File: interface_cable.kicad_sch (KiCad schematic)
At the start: 18 parts

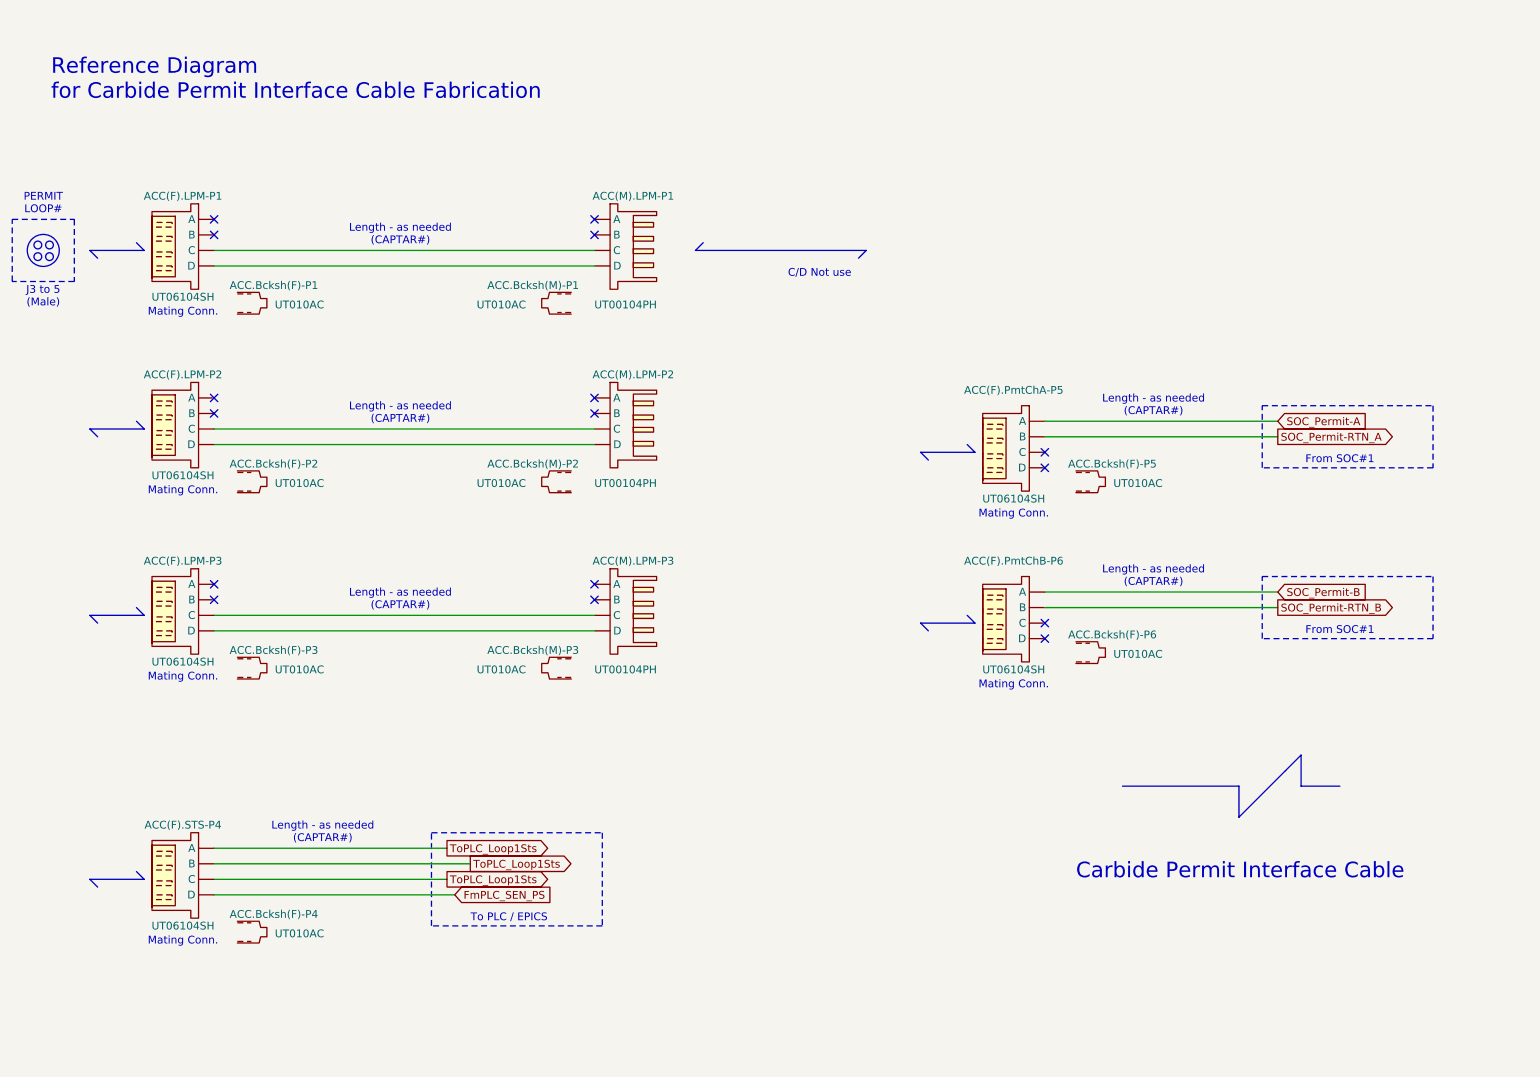
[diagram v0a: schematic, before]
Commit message: Updated Interface cable
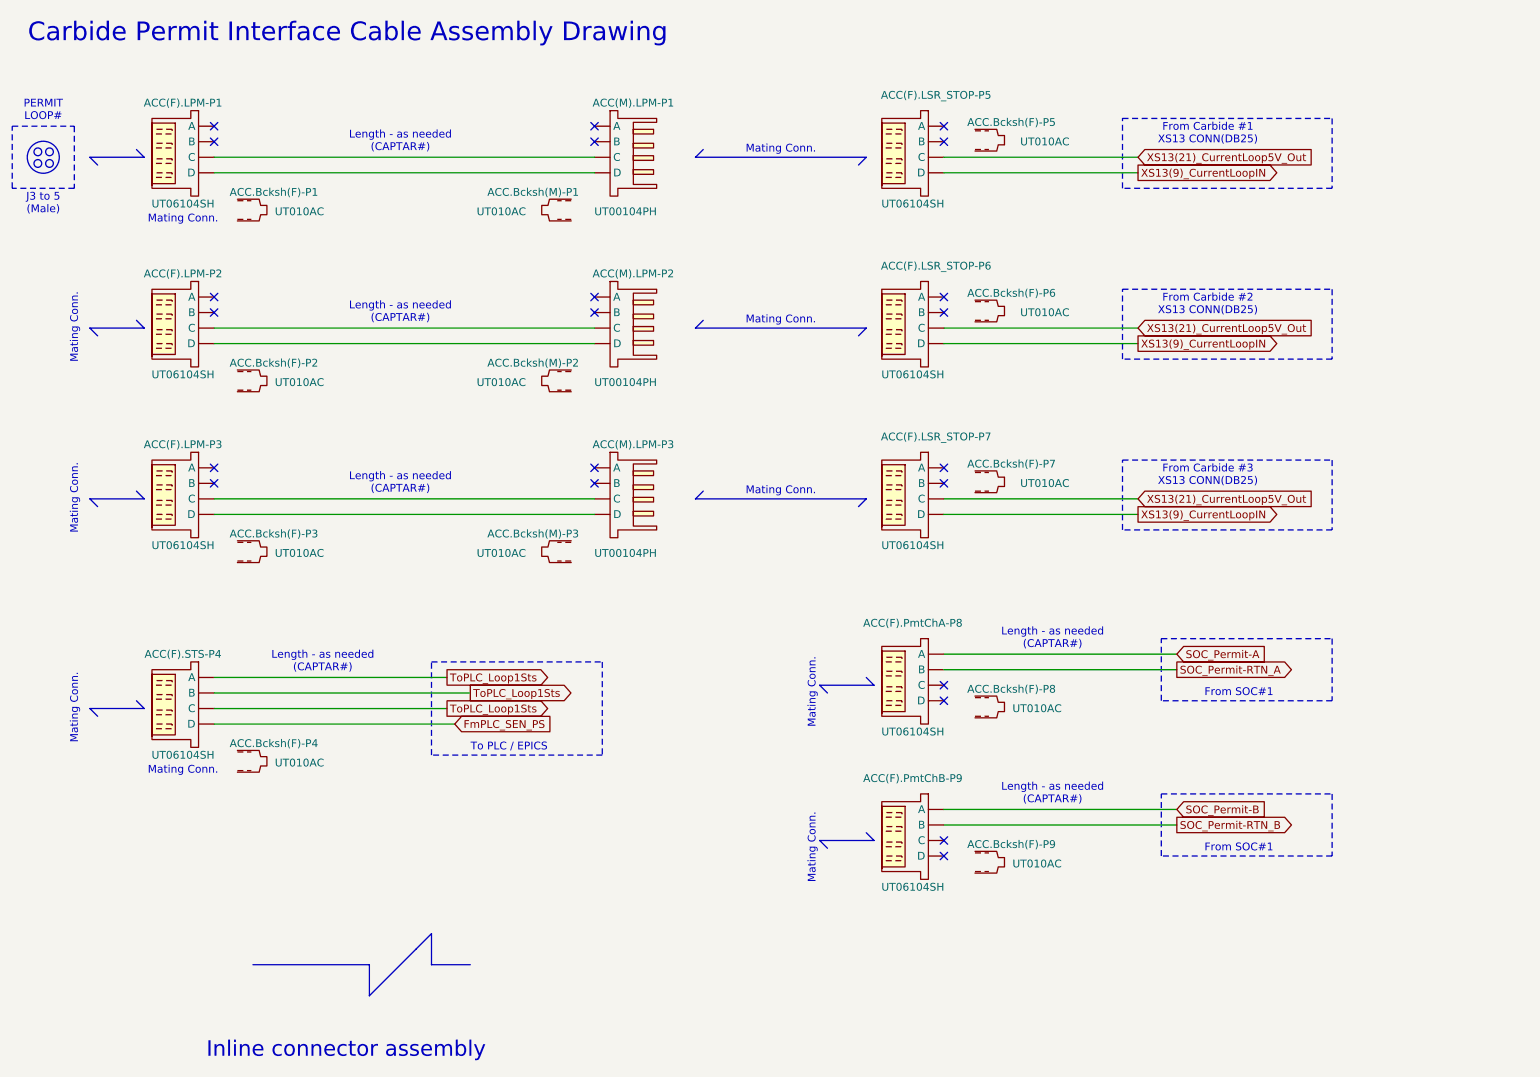
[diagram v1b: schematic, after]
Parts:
- added ACC(F).LSR_STOP-P5, ACC(F).LSR_STOP-P6, ACC(F).LSR_STOP-P7: UT06104SH, symbol JP_3xCarbide:CONN_UT00104SH(F)
- added ACC.Bcksh(F)-P5, ACC.Bcksh(F)-P6, ACC.Bcksh(F)-P7: UT010AC, symbol JP_3xCarbide:Bcksh_/_Clamp
- renumbered ACC(F).PmtChA-P5 to ACC(F).PmtChA-P8, ACC(F).PmtChB-P6 to ACC(F).PmtChB-P9, ACC.Bcksh(F)-P5 to ACC.Bcksh(F)-P8, ACC.Bcksh(F)-P6 to ACC.Bcksh(F)-P9
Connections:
- net at ACC(F).LPM-P2. (D): now also ACC(M).LPM-P2. (D)
- net at ACC(M).LPM-P2. (D): no longer ACC(F).LPM-P2. (D)
- net at ACC(F).LPM-P3. (D): now also ACC(M).LPM-P3. (D)
- net at ACC(M).LPM-P3. (D): no longer ACC(F).LPM-P3. (D)
- net at ACC(M).LPM-P1. (D): now also ACC(F).LPM-P1. (D)
- net at ACC(F).LPM-P1. (D): no longer ACC(M).LPM-P1. (D)
- new net: ACC(F).LPM-P2. (D), ACC(M).LPM-P2. (D)
- new net: ACC(F).LPM-P3. (D), ACC(M).LPM-P3. (D)
- new net: ACC(F).LPM-P1. (D), ACC(M).LPM-P1. (D)
- new net XS13(21)_CurrentLoop5V_Out: ACC(F).LSR_STOP-P5. (D), ACC(F).LSR_STOP-P6. (D), ACC(F).LSR_STOP-P7. (D)
- new net XS13(9)_CurrentLoopIN: ACC(F).LSR_STOP-P5. (D), ACC(F).LSR_STOP-P6. (D), ACC(F).LSR_STOP-P7. (D)
- now unconnected: ACC(F).LPM-P1. (D), ACC(M).LPM-P2. (D), ACC(M).LPM-P3. (D)
- no-connect marks 16 -> 22
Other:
- note added: "Carbide Permit Interface Cable Assembly Drawing"
- note added: "From Carbide #1 XS13 CONN(DB25)"
- note added: "From Carbide #2 XS13 CONN(DB25)"
- note added: "From Carbide #3 XS13 CONN(DB25)"
- note added: "Inline connector assembly"
- note removed: "C/D Not use"
- note removed: "Carbide Permit Interface Cable"
- note removed: "Reference Diagram for Carbide Permit Interface Cable Fabrication"
- moved on the sheet: ACC(F).LPM-P1, ACC(F).LPM-P2, ACC(F).LPM-P3, ACC(F).PmtChA-P8, ACC(F).PmtChB-P9, ACC(F).STS-P4, ACC(M).LPM-P1, ACC(M).LPM-P2, ACC(M).LPM-P3, ACC.Bcksh(F)-P1, ACC.Bcksh(F)-P2, ACC.Bcksh(F)-P3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

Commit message: Clean up
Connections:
- net at ACC(F).LPM-P2. (D): now also ACC(M).LPM-P2. (D)
- net at ACC(M).LPM-P2. (D): no longer ACC(F).LPM-P2. (D)
- net at ACC(F).LPM-P3. (D): now also ACC(M).LPM-P3. (D)
- net at ACC(M).LPM-P3. (D): no longer ACC(F).LPM-P3. (D)
- net at ACC(M).LPM-P1. (D): now also ACC(F).LPM-P1. (D)
- net at ACC(F).LPM-P1. (D): no longer ACC(M).LPM-P1. (D)
- new net: ACC(F).LPM-P2. (D), ACC(M).LPM-P2. (D)
- new net: ACC(F).LPM-P3. (D), ACC(M).LPM-P3. (D)
- new net: ACC(F).LPM-P1. (D), ACC(M).LPM-P1. (D)
- now unconnected: ACC(F).LPM-P1. (D), ACC(M).LPM-P2. (D), ACC(M).LPM-P3. (D)
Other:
- note added: "(Length - as needed)"
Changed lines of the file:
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@@
 		)
 	)
+	(text "(Length - as needed)"
+		(exclude_from_sim no)
+		(at 194.31 102.87 0)
+		(effects
+			(font
+				(size 1.27 1.27)
+			)
+		)
+	)
 	(text "Length - as needed\n(CAPTAR#)"
 		(exclude_from_sim no)
@@
 		)
 	)
+	(text "(Length - as needed)"
+		(exclude_from_sim no)
+		(at 193.04 46.99 0)
+		(effects
+			(font
+				(size 1.27 1.27)
+			)
+		)
+	)
 	(text "From SOC#1"
 		(exclude_from_sim no)
@@
 		)
 	)
+	(text "(Length - as needed)"
+		(exclude_from_sim no)
+		(at 193.04 74.93 0)
+		(effects
+			(font
+				(size 1.27 1.27)
+			)
+		)
+	)
 	(text "Inline connector assembly"
 		(exclude_from_sim no)
-		(at 58.42 189.23 0)
+		(at 59.69 187.96 0)
 		(effects
 			(font
@@
 	(polyline
 		(pts
-			(xy 95.25 175.26) (xy 101.6 175.26)
+			(xy 96.52 173.99) (xy 102.87 173.99)
 		)
 		(stroke
@@
 	(polyline
 		(pts
-			(xy 95.25 170.18) (xy 95.25 175.26)
+			(xy 96.52 168.91) (xy 96.52 173.99)
 		)
 		(stroke
@@
 	(polyline
 		(pts
-			(xy 66.04 175.26) (xy 85.09 175.26)
+			(xy 67.31 173.99) (xy 86.36 173.99)
 		)
 		(stroke
@@
 	(polyline
 		(pts
-			(xy 85.09 175.26) (xy 85.09 180.34)
+			(xy 86.36 173.99) (xy 86.36 179.07)
 		)
 		(stroke
@@
 	(polyline
 		(pts
-			(xy 92.71 172.72) (xy 95.25 170.18)
+			(xy 93.98 171.45) (xy 96.52 168.91)
 		)
 		(stroke
@@
 	(polyline
 		(pts
-			(xy 85.09 180.34) (xy 92.71 172.72)
+			(xy 86.36 179.07) (xy 93.98 171.45)
 		)
 		(stroke
@@
 	)
 	(image
-		(at 55.88 176.53)
+		(at 57.15 175.26)
 		(scale 0.0825803)
 		(data "iVBORw0KGgoAAAANSUhEUgAAApwAAAHdCAIAAAA/xT6mAAAAA3NCSVQICAjb4U/gAAAACXBIWXMA"
@@
 	)
 	(image
-		(at 40.64 176.53)
+		(at 41.91 175.26)
 		(scale 0.0700208)
 		(data "iVBORw0KGgoAAAANSUhEUgAAAo0AAAIvCAIAAACeG3b/AAAAA3NCSVQICAjb4U/gAAAACXBIWXMA"
@@
 	)
 	(image
-		(at 127 176.53)
+		(at 128.27 175.26)
 		(scale 0.112786)
 		(data "iVBORw0KGgoAAAANSUhEUgAAAhAAAAHlCAIAAAAr1VLpAAAAA3NCSVQICAjb4U/gAAAACXBIWXMA"
@@
 	)
 	(image
-		(at 110.49 176.53)
+		(at 111.76 175.26)
 		(scale 0.08258)
 		(data "iVBORw0KGgoAAAANSUhEUgAAApwAAAHdCAIAAAA/xT6mAAAAA3NCSVQICAjb4U/gAAAACXBIWXMA"

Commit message: Updated PS and clean up
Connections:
- net at ACC(F).LPM-P2. (D): now also ACC(M).LPM-P2. (D)
- net at ACC(M).LPM-P2. (D): no longer ACC(F).LPM-P2. (D)
- net at ACC(F).LPM-P3. (D): now also ACC(M).LPM-P3. (D)
- net at ACC(M).LPM-P3. (D): no longer ACC(F).LPM-P3. (D)
- net at ACC(M).LPM-P1. (D): now also ACC(F).LPM-P1. (D)
- net at ACC(F).LPM-P1. (D): no longer ACC(M).LPM-P1. (D)
- new net: ACC(F).LPM-P2. (D), ACC(M).LPM-P2. (D)
- new net: ACC(F).LPM-P3. (D), ACC(M).LPM-P3. (D)
- new net: ACC(F).LPM-P1. (D), ACC(M).LPM-P1. (D)
- now unconnected: ACC(F).LPM-P1. (D), ACC(M).LPM-P2. (D), ACC(M).LPM-P3. (D)
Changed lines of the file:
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@@
 		(title "LCLS-II BCS CARBIDE PERMIT INTERLOCK")
 		(date "2026-08-21")
-		(rev "1.01")
+		(rev "1.02")
 		(company "SLAC")
 		(comment 1 "ENGR: J.Park")

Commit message: updated SSR Pin and cleanup
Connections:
- net at ACC(F).LPM-P2. (D): now also ACC(M).LPM-P2. (D)
- net at ACC(M).LPM-P2. (D): no longer ACC(F).LPM-P2. (D)
- net at ACC(F).LPM-P3. (D): now also ACC(M).LPM-P3. (D)
- net at ACC(M).LPM-P3. (D): no longer ACC(F).LPM-P3. (D)
- net at ACC(M).LPM-P1. (D): now also ACC(F).LPM-P1. (D)
- net at ACC(F).LPM-P1. (D): no longer ACC(M).LPM-P1. (D)
- new net: ACC(F).LPM-P2. (D), ACC(M).LPM-P2. (D)
- new net: ACC(F).LPM-P3. (D), ACC(M).LPM-P3. (D)
- new net: ACC(F).LPM-P1. (D), ACC(M).LPM-P1. (D)
- now unconnected: ACC(F).LPM-P1. (D), ACC(M).LPM-P2. (D), ACC(M).LPM-P3. (D)
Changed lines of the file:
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@@
 		(title "LCLS-II BCS CARBIDE PERMIT INTERLOCK")
 		(date "2026-08-21")
-		(rev "1.02")
+		(rev "1.03")
 		(company "SLAC")
 		(comment 1 "ENGR: J.Park")

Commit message: updated 3input-SSR Lib
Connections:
- net at ACC(F).LPM-P2. (D): now also ACC(M).LPM-P2. (D)
- net at ACC(M).LPM-P2. (D): no longer ACC(F).LPM-P2. (D)
- net at ACC(F).LPM-P3. (D): now also ACC(M).LPM-P3. (D)
- net at ACC(M).LPM-P3. (D): no longer ACC(F).LPM-P3. (D)
- net at ACC(M).LPM-P1. (D): now also ACC(F).LPM-P1. (D)
- net at ACC(F).LPM-P1. (D): no longer ACC(M).LPM-P1. (D)
- new net: ACC(F).LPM-P2. (D), ACC(M).LPM-P2. (D)
- new net: ACC(F).LPM-P3. (D), ACC(M).LPM-P3. (D)
- new net: ACC(F).LPM-P1. (D), ACC(M).LPM-P1. (D)
- now unconnected: ACC(F).LPM-P1. (D), ACC(M).LPM-P2. (D), ACC(M).LPM-P3. (D)
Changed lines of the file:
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@@
 		(title "LCLS-II BCS CARBIDE PERMIT INTERLOCK")
 		(date "2026-08-21")
-		(rev "1.03")
+		(rev "1.04")
 		(company "SLAC")
 		(comment 1 "ENGR: J.Park")
